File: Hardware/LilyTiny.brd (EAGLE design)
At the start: 20 x 20 mm, 13 parts, among them U1 ATTINY85

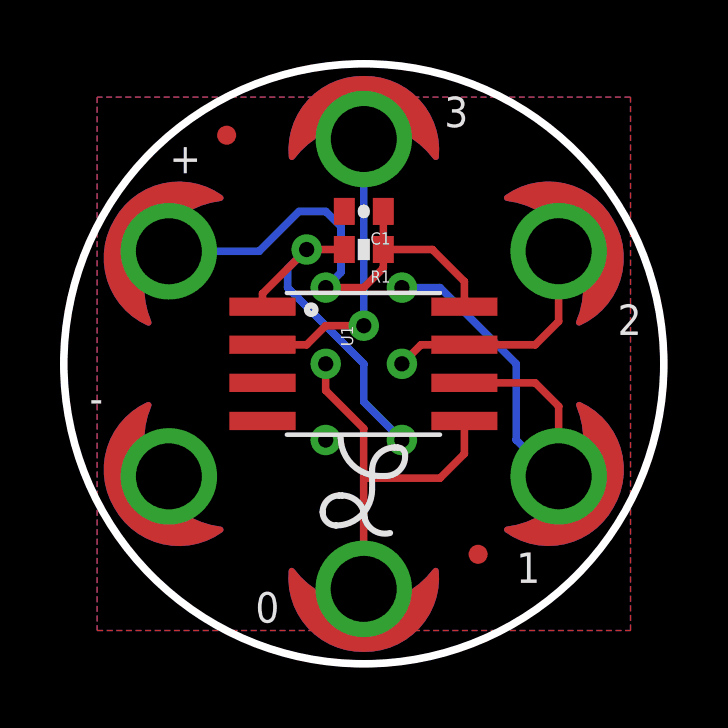
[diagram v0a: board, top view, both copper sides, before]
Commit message: Moved components to 0603 package size
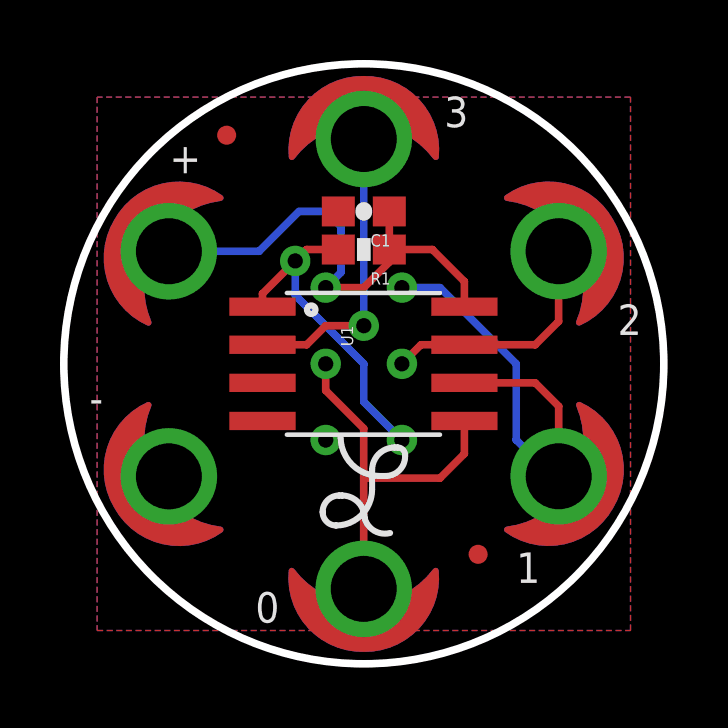
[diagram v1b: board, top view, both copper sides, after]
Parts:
- C1: device SparkFun:0402-CAP -> SparkFun:0603-CAP
- R1: device SparkFun:0402-RES -> SparkFun:0603-RES
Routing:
- net NRESET: track 12.0 -> 11.0 mm
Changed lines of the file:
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@@
 <grid distance="0.05" unitdist="inch" unit="inch" style="lines" multiple="1" display="yes" altdistance="0.005" altunitdist="inch" altunit="inch"/>
 <layers>
-<layer number="1" name="Top" color="4" fill="1" visible="no" active="yes"/>
+<layer number="1" name="Top" color="4" fill="1" visible="yes" active="yes"/>
 <layer number="2" name="Route2" color="1" fill="3" visible="no" active="no"/>
 <layer number="3" name="Route3" color="4" fill="3" visible="no" active="no"/>
@@
 <layer number="17" name="Pads" color="2" fill="1" visible="yes" active="yes"/>
 <layer number="18" name="Vias" color="2" fill="1" visible="yes" active="yes"/>
-<layer number="19" name="Unrouted" color="6" fill="1" visible="no" active="yes"/>
+<layer number="19" name="Unrouted" color="6" fill="1" visible="yes" active="yes"/>
 <layer number="20" name="Dimension" color="6" fill="1" visible="yes" active="yes"/>
-<layer number="21" name="tPlace" color="16" fill="1" visible="no" active="yes"/>
+<layer number="21" name="tPlace" color="16" fill="1" visible="yes" active="yes"/>
 <layer number="22" name="bPlace" color="14" fill="1" visible="yes" active="yes"/>
-<layer number="23" name="tOrigins" color="15" fill="1" visible="no" active="yes"/>
-<layer number="24" name="bOrigins" color="15" fill="1" visible="no" active="yes"/>
+<layer number="23" name="tOrigins" color="15" fill="1" visible="yes" active="yes"/>
+<layer number="24" name="bOrigins" color="15" fill="1" visible="yes" active="yes"/>
 <layer number="25" name="tNames" color="7" fill="1" visible="no" active="yes"/>
 <layer number="26" name="bNames" color="7" fill="1" visible="no" active="yes"/>
@@
 <layer number="28" name="bValues" color="7" fill="1" visible="no" active="yes"/>
 <layer number="29" name="tStop" color="7" fill="3" visible="no" active="yes"/>
-<layer number="30" name="bStop" color="7" fill="6" visible="yes" active="yes"/>
+<layer number="30" name="bStop" color="7" fill="6" visible="no" active="yes"/>
 <layer number="31" name="tCream" color="7" fill="4" visible="no" active="yes"/>
 <layer number="32" name="bCream" color="7" fill="5" visible="no" active="yes"/>
@@
 <layer number="43" name="vRestrict" color="2" fill="10" visible="no" active="yes"/>
 <layer number="44" name="Drills" color="7" fill="1" visible="no" active="yes"/>
-<layer number="45" name="Holes" color="7" fill="1" visible="no" active="yes"/>
+<layer number="45" name="Holes" color="7" fill="1" visible="yes" active="yes"/>
 <layer number="46" name="Milling" color="3" fill="1" visible="no" active="yes"/>
 <layer number="47" name="Measures" color="7" fill="1" visible="no" active="yes"/>
 <layer number="48" name="Document" color="7" fill="1" visible="no" active="yes"/>
-<layer number="49" name="Reference" color="7" fill="1" visible="no" active="yes"/>
+<layer number="49" name="Reference" color="7" fill="1" visible="yes" active="yes"/>
 <layer number="50" name="dxf" color="7" fill="1" visible="no" active="yes"/>
-<layer number="51" name="tDocu" color="6" fill="1" visible="no" active="yes"/>
+<layer number="51" name="tDocu" color="6" fill="1" visible="yes" active="yes"/>
 <layer number="52" name="bDocu" color="7" fill="1" visible="no" active="yes"/>
 <layer number="53" name="tGND_GNDA" color="7" fill="9" visible="no" active="no"/>
@@
 <elements>
 <element name="U1" library="SparkFun" package="SO08-EIAJ" value="ATTINY85" x="0" y="0" rot="R270"/>
-<element name="C1" library="SparkFun" package="0402-CAP" value="0.1uF" x="0" y="5.08" rot="R180"/>
-<element name="R1" library="SparkFun" package="0402-RES" value="10k" x="0" y="3.81" rot="R180"/>
+<element name="C1" library="SparkFun" package="0603-CAP" value="0.1uF" x="0" y="5.08" rot="R180"/>
+<element name="R1" library="SparkFun" package="0603-RES" value="10k" x="0" y="3.81" rot="R180"/>
 <element name="U$2" library="LilyPad-Wearables" package="PETAL-SMALL-2SIDE" value="SEWTAP6" x="-6.4976" y="-3.7514" rot="R300"/>
 <element name="U$3" library="LilyPad-Wearables" package="PETAL-SMALL-2SIDE" value="SEWTAP6" x="6.4962" y="-3.7491" rot="R60"/>
@@
 <wire x1="3.3528" y1="2.7432" x2="3.3528" y2="1.905" width="0.254" layer="1"/>
 <wire x1="2.286" y1="3.81" x2="3.3528" y2="2.7432" width="0.254" layer="1"/>
-<wire x1="0.65" y1="3.81" x2="2.286" y2="3.81" width="0.254" layer="1"/>
-<wire x1="0.65" y1="5.08" x2="0.65" y2="3.81" width="0.254" layer="1"/>
-<wire x1="0.65" y1="3.81" x2="0.65" y2="3.19" width="0.254" layer="1"/>
-<wire x1="0.65" y1="3.19" x2="0" y2="2.54" width="0.254" layer="1"/>
+<wire x1="0.85" y1="3.81" x2="2.286" y2="3.81" width="0.254" layer="1"/>
+<wire x1="0.85" y1="5.08" x2="0.85" y2="3.81" width="0.254" layer="1"/>
 <wire x1="0" y1="2.54" x2="-1.27" y2="2.54" width="0.254" layer="1"/>
 <via x="-1.27" y="2.54" extent="1-16" drill="0.508"/>
@@
 <wire x1="-2.159" y1="5.08" x2="-3.4875" y2="3.7515" width="0.254" layer="16"/>
 <wire x1="-6.4975" y1="3.7515" x2="-3.4875" y2="3.7515" width="0.254" layer="16"/>
+<wire x1="0" y1="2.54" x2="0.85" y2="3.39" width="0.254" layer="1"/>
+<wire x1="0.85" y1="3.39" x2="0.85" y2="3.81" width="0.254" layer="1"/>
 </signal>
 <signal name="NRESET">
@@
 <contactref element="U1" pad="1"/>
 <via x="1.27" y="-2.54" extent="1-16" drill="0.508"/>
-<via x="-1.905" y="3.81" extent="1-16" drill="0.508"/>
-<wire x1="-0.65" y1="3.81" x2="-1.905" y2="3.81" width="0.254" layer="1"/>
-<wire x1="-1.905" y1="3.81" x2="-3.3782" y2="2.3368" width="0.254" layer="1"/>
-<wire x1="-3.3782" y1="1.905" x2="-3.3782" y2="2.3368" width="0.254" layer="1"/>
-<wire x1="-1.905" y1="3.81" x2="-2.54" y2="3.175" width="0.254" layer="16"/>
-<wire x1="-2.54" y1="3.175" x2="-2.54" y2="2.54" width="0.254" layer="16"/>
-<wire x1="-2.54" y1="2.54" x2="0" y2="0" width="0.254" layer="16"/>
+<via x="-2.286" y="3.429" extent="1-16" drill="0.508"/>
 <wire x1="0" y1="0" x2="0" y2="-1.27" width="0.254" layer="16"/>
 <wire x1="0" y1="-1.27" x2="1.27" y2="-2.54" width="0.254" layer="16"/>
+<wire x1="-0.85" y1="3.81" x2="-1.905" y2="3.81" width="0.254" layer="1"/>
+<wire x1="-1.905" y1="3.81" x2="-2.286" y2="3.429" width="0.254" layer="1"/>
+<wire x1="-3.3782" y1="1.905" x2="-3.3782" y2="2.3368" width="0.254" layer="1"/>
+<wire x1="-3.3782" y1="2.3368" x2="-2.286" y2="3.429" width="0.254" layer="1"/>
+<wire x1="0" y1="0" x2="-2.286" y2="2.286" width="0.254" layer="16"/>
+<wire x1="-2.286" y1="2.286" x2="-2.286" y2="3.429" width="0.254" layer="16"/>
 </signal>
 <signal name="GND">

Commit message: Moved to 0603 components, added OSHW logo
-moved R1 and C1 a bit to fit in 0603 packages. Had to re-route some
traces.
-Added OSHW.
-Updated Frame.
-added version to both sch and brd
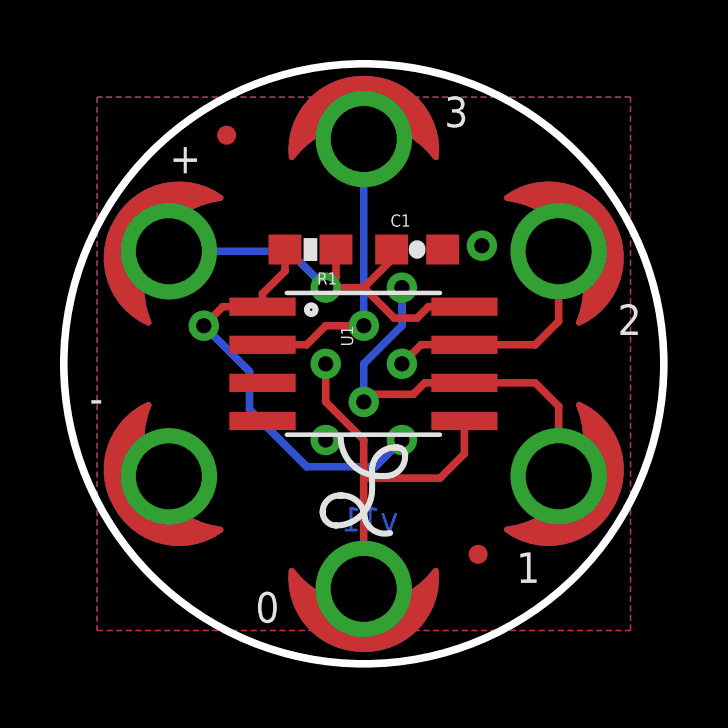
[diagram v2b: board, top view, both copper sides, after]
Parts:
- removed U$1: CREATIVE_COMMONS, SparkFun:CREATIVE_COMMONS
- added FRAME2: FRAME-LETTER, SparkFun-Aesthetics:CREATIVE_COMMONS
- added LOGO1: OSHW-LOGOS, SparkFun-Aesthetics:OSHW-LOGO-S
- moved C1 2.18 mm to (1.78, 3.81), turned to 0 degrees
- moved R1 1.78 mm to (-1.78, 3.81)
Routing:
- net N$9: track 4.86 -> 0.00 mm, vias 1 -> 0
- net N$4: track 10.3 -> 14.0 mm, vias 0 -> 2
- net NRESET: track 11.0 -> 14.1 mm
- net VCC: track 16.7 -> 14.0 mm
- net N$3: vias 0 -> 1
- net N$5: vias 0 -> 1
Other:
- board text added: "Revised by Pete Lewis"
- board text added: "v11"
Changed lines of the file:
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@@
 <layer number="144" name="Drill_legend" color="7" fill="1" visible="no" active="yes"/>
 <layer number="151" name="HeatSink" color="7" fill="1" visible="no" active="yes"/>
+<layer number="199" name="Contour" color="7" fill="1" visible="no" active="yes"/>
 <layer number="200" name="200bmp" color="1" fill="10" visible="no" active="yes"/>
 <layer number="201" name="201bmp" color="2" fill="10" visible="no" active="yes"/>
@@
 <text x="8.4602" y="0.962" size="1.016" layer="21" font="vector" ratio="15">2</text>
 <text x="-9.144" y="-1.651" size="1.016" layer="21" font="vector" ratio="15">-</text>
-<text x="43.18" y="-24.13" size="1.778" layer="27" font="vector" ratio="15">M. HORD</text>
+<text x="40.64" y="-33.02" size="1.27" layer="27" font="vector" ratio="15">M. HORD</text>
 <polygon width="0.2032" layer="29">
 <vertex x="-6" y="0"/>
@@
 <rectangle x1="2.54" y1="-2.286" x2="3.429" y2="-1.397" layer="22"/>
 <rectangle x1="4.064" y1="-2.286" x2="4.953" y2="-1.397" layer="22"/>
+<text x="1.143" y="-5.588" size="0.8128" layer="16" font="vector" ratio="25" rot="MR0">v11</text>
+<text x="49.53" y="-33.02" size="1.27" layer="27" font="vector" ratio="15">Revised by Pete Lewis</text>
 </plain>
 <attributes>
@@
 <elements>
 <element name="U1" library="SparkFun" package="SO08-EIAJ" value="ATTINY85" x="0" y="0" rot="R270"/>
-<element name="C1" library="SparkFun" package="0603-CAP" value="0.1uF" x="0" y="5.08" rot="R180"/>
-<element name="R1" library="SparkFun" package="0603-RES" value="10k" x="0" y="3.81" rot="R180"/>
+<element name="C1" library="SparkFun" package="0603-CAP" value="0.1uF" x="1.778" y="3.81"/>
+<element name="R1" library="SparkFun" package="0603-RES" value="10k" x="-1.778" y="3.81" rot="R180"/>
 <element name="U$2" library="LilyPad-Wearables" package="PETAL-SMALL-2SIDE" value="SEWTAP6" x="-6.4976" y="-3.7514" rot="R300"/>
 <element name="U$3" library="LilyPad-Wearables" package="PETAL-SMALL-2SIDE" value="SEWTAP6" x="6.4962" y="-3.7491" rot="R60"/>
@@
 <element name="U$6" library="LilyPad-Wearables" package="PETAL-SMALL-2SIDE" value="SEWTAP6" x="0" y="7.493" rot="R180"/>
 <element name="U$7" library="LilyPad-Wearables" package="PETAL-SMALL-2SIDE" value="SEWTAP6" x="-0.0034" y="-7.502"/>
-<element name="U$1" library="SparkFun" package="CREATIVE_COMMONS" value="CREATIVE_COMMONS" x="11.43" y="-24.13"/>
 <element name="U$8" library="LilyPad-Wearables" package="LOGO-L" value="LOGO-LPL" x="0" y="-4.064"/>
 <element name="JP1" library="SparkFun" package="MICRO-FIDUCIAL" value="FIDUCIALUFIDUCIAL" x="-4.572" y="7.62"/>
 <element name="JP2" library="SparkFun" package="MICRO-FIDUCIAL" value="FIDUCIALUFIDUCIAL" x="3.81" y="-6.35"/>
+<element name="FRAME2" library="SparkFun-Aesthetics" package="CREATIVE_COMMONS" value="FRAME-LETTER" x="10.16" y="-33.02"/>
+<element name="LOGO1" library="SparkFun-Aesthetics" package="OSHW-LOGO-S" value="OSHW-LOGOS" x="-3.81" y="0" rot="MR90"/>
 </elements>
 <signals>
@@
 <contactref element="U1" pad="8"/>
 <contactref element="C1" pad="1"/>
-<wire x1="3.3528" y1="2.7432" x2="3.3528" y2="1.905" width="0.254" layer="1"/>
-<wire x1="2.286" y1="3.81" x2="3.3528" y2="2.7432" width="0.254" layer="1"/>
-<wire x1="0.85" y1="3.81" x2="2.286" y2="3.81" width="0.254" layer="1"/>
-<wire x1="0.85" y1="5.08" x2="0.85" y2="3.81" width="0.254" layer="1"/>
 <wire x1="0" y1="2.54" x2="-1.27" y2="2.54" width="0.254" layer="1"/>
 <via x="-1.27" y="2.54" extent="1-16" drill="0.508"/>
 <contactref element="U$5" pad="1"/>
-<wire x1="-1.27" y1="2.54" x2="-0.762" y2="3.048" width="0.254" layer="16"/>
-<wire x1="-0.762" y1="3.048" x2="-0.762" y2="4.572" width="0.254" layer="16"/>
-<wire x1="-0.762" y1="4.572" x2="-1.27" y2="5.08" width="0.254" layer="16"/>
-<wire x1="-1.27" y1="5.08" x2="-2.159" y2="5.08" width="0.254" layer="16"/>
-<wire x1="-2.159" y1="5.08" x2="-3.4875" y2="3.7515" width="0.254" layer="16"/>
-<wire x1="-6.4975" y1="3.7515" x2="-3.4875" y2="3.7515" width="0.254" layer="16"/>
-<wire x1="0" y1="2.54" x2="0.85" y2="3.39" width="0.254" layer="1"/>
-<wire x1="0.85" y1="3.39" x2="0.85" y2="3.81" width="0.254" layer="1"/>
+<wire x1="-0.928" y1="3.81" x2="-0.928" y2="2.882" width="0.254" layer="1"/>
+<wire x1="-0.928" y1="2.882" x2="-1.27" y2="2.54" width="0.254" layer="1"/>
+<wire x1="-6.4975" y1="3.7515" x2="-2.4815" y2="3.7515" width="0.254" layer="16"/>
+<wire x1="-2.4815" y1="3.7515" x2="-1.27" y2="2.54" width="0.254" layer="16"/>
+<wire x1="3.3528" y1="1.905" x2="2.159" y2="1.905" width="0.254" layer="1"/>
+<wire x1="2.159" y1="1.905" x2="1.778" y2="1.524" width="0.254" layer="1"/>
+<wire x1="1.778" y1="1.524" x2="1.016" y2="1.524" width="0.254" layer="1"/>
+<wire x1="1.016" y1="1.524" x2="0" y2="2.54" width="0.254" layer="1"/>
+<wire x1="0" y1="2.54" x2="0.928" y2="3.468" width="0.254" layer="1"/>
+<wire x1="0.928" y1="3.468" x2="0.928" y2="3.81" width="0.254" layer="1"/>
 </signal>
 <signal name="NRESET">
@@
 <contactref element="U1" pad="1"/>
 <via x="1.27" y="-2.54" extent="1-16" drill="0.508"/>
-<via x="-2.286" y="3.429" extent="1-16" drill="0.508"/>
-<wire x1="0" y1="0" x2="0" y2="-1.27" width="0.254" layer="16"/>
-<wire x1="0" y1="-1.27" x2="1.27" y2="-2.54" width="0.254" layer="16"/>
-<wire x1="-0.85" y1="3.81" x2="-1.905" y2="3.81" width="0.254" layer="1"/>
-<wire x1="-1.905" y1="3.81" x2="-2.286" y2="3.429" width="0.254" layer="1"/>
 <wire x1="-3.3782" y1="1.905" x2="-3.3782" y2="2.3368" width="0.254" layer="1"/>
-<wire x1="-3.3782" y1="2.3368" x2="-2.286" y2="3.429" width="0.254" layer="1"/>
-<wire x1="0" y1="0" x2="-2.286" y2="2.286" width="0.254" layer="16"/>
-<wire x1="-2.286" y1="2.286" x2="-2.286" y2="3.429" width="0.254" layer="16"/>
+<wire x1="-3.81" y1="-0.254" x2="-5.334" y2="1.27" width="0.254" layer="16"/>
+<via x="-5.334" y="1.27" extent="1-16" drill="0.508"/>
+<wire x1="-5.334" y1="1.27" x2="-4.699" y2="1.905" width="0.254" layer="1"/>
+<wire x1="-4.699" y1="1.905" x2="-3.3782" y2="1.905" width="0.254" layer="1"/>
+<wire x1="-3.3782" y1="2.3368" x2="-2.628" y2="3.087" width="0.254" layer="1"/>
+<wire x1="-2.628" y1="3.087" x2="-2.628" y2="3.81" width="0.254" layer="1"/>
+<wire x1="1.27" y1="-2.54" x2="0.381" y2="-3.429" width="0.254" layer="16"/>
+<wire x1="0.381" y1="-3.429" x2="-1.905" y2="-3.429" width="0.254" layer="16"/>
+<wire x1="-1.905" y1="-3.429" x2="-3.81" y2="-1.524" width="0.254" layer="16"/>
+<wire x1="-3.81" y1="-1.524" x2="-3.81" y2="-0.254" width="0.254" layer="16"/>
 </signal>
 <signal name="GND">
@@
 <via x="-1.27" y="-2.54" extent="1-16" drill="0.508"/>
 <contactref element="U$2" pad="1"/>
+<via x="3.937" y="3.937" extent="1-16" drill="0.508"/>
 </signal>
 <signal name="N$3">
 <contactref element="U1" pad="5"/>
 <contactref element="U$7" pad="1"/>
-<wire x1="-1.27" y1="-0.889" x2="-1.27" y2="0" width="0.254" layer="1"/>
+<wire x1="-1.27" y1="-1.27" x2="-1.27" y2="0" width="0.254" layer="1"/>
 <wire x1="-0.0034" y1="-7.502" x2="-0.0034" y2="-3.81" width="0.254" layer="1"/>
 <wire x1="3.3528" y1="-1.905" x2="3.3528" y2="-2.9972" width="0.254" layer="1"/>
 <wire x1="3.3528" y1="-2.9972" x2="2.54" y2="-3.81" width="0.254" layer="1"/>
 <wire x1="2.54" y1="-3.81" x2="-0.0034" y2="-3.81" width="0.254" layer="1"/>
-<wire x1="-0.0034" y1="-3.81" x2="-0.0034" y2="-2.1556" width="0.254" layer="1"/>
-<wire x1="-0.0034" y1="-2.1556" x2="-1.27" y2="-0.889" width="0.254" layer="1"/>
+<wire x1="-0.0034" y1="-3.81" x2="-0.0034" y2="-2.5366" width="0.254" layer="1"/>
+<wire x1="-0.0034" y1="-2.5366" x2="-1.27" y2="-1.27" width="0.254" layer="1"/>
+<via x="-1.27" y="0" extent="1-16" drill="0.508"/>
 </signal>
 <signal name="N$4">
@@
 <wire x1="6.4962" y1="-3.7491" x2="6.4962" y2="-1.4162" width="0.254" layer="1"/>
 <wire x1="6.4962" y1="-3.7491" x2="6.2891" y2="-3.7491" width="0.254" layer="16"/>
-<wire x1="6.2891" y1="-3.7491" x2="5.08" y2="-2.54" width="0.254" layer="16"/>
-<wire x1="5.08" y1="-2.54" x2="5.08" y2="0" width="0.254" layer="16"/>
+<via x="1.27" y="2.54" extent="1-16" drill="0.508"/>
+<via x="0" y="-1.27" extent="1-16" drill="0.508"/>
+<wire x1="3.3528" y1="-0.635" x2="2.032" y2="-0.635" width="0.254" layer="1"/>
+<wire x1="2.032" y1="-0.635" x2="1.651" y2="-1.016" width="0.254" layer="1"/>
+<wire x1="1.651" y1="-1.016" x2="0.254" y2="-1.016" width="0.254" layer="1"/>
+<wire x1="0.254" y1="-1.016" x2="0" y2="-1.27" width="0.254" layer="1"/>
+<wire x1="1.27" y1="2.54" x2="1.27" y2="1.27" width="0.254" layer="16"/>
+<wire x1="1.27" y1="1.27" x2="0" y2="0" width="0.254" layer="16"/>
+<wire x1="0" y1="0" x2="0" y2="-1.27" width="0.254" layer="16"/>
 </signal>
 <signal name="N$5">
@@
 <wire x1="5.715" y1="0.635" x2="6.494" y2="1.414" width="0.254" layer="1"/>
 <wire x1="6.494" y1="3.7535" x2="6.494" y2="1.414" width="0.254" layer="1"/>
+<via x="1.27" y="0" extent="1-16" drill="0.508"/>
 </signal>
 <signal name="N$6">
@@
 <wire x1="0" y1="7.493" x2="0" y2="1.27" width="0.254" layer="16"/>
 </signal>
-<signal name="N$7">
-<via x="-1.27" y="0" extent="1-16" drill="0.508"/>
-</signal>
-<signal name="N$8">
-<via x="1.27" y="0" extent="1-16" drill="0.508"/>
-</signal>
-<signal name="N$9">
-<via x="1.27" y="2.54" extent="1-16" drill="0.508"/>
-<wire x1="1.27" y1="2.54" x2="2.54" y2="2.54" width="0.254" layer="16"/>
-<wire x1="2.54" y1="2.54" x2="5.08" y2="0" width="0.254" layer="16"/>
-</signal>
 <signal name="N$1">
